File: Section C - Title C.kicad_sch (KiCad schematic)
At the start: 6 parts, among them J11 Conn_01x02_Socket, J2 Conn_01x07_Socket, J6 Conn_01x03_Socket, J7 Conn_01x04_Socket, J8 Conn_01x03_Socket, J9 Conn_01x03_Socket

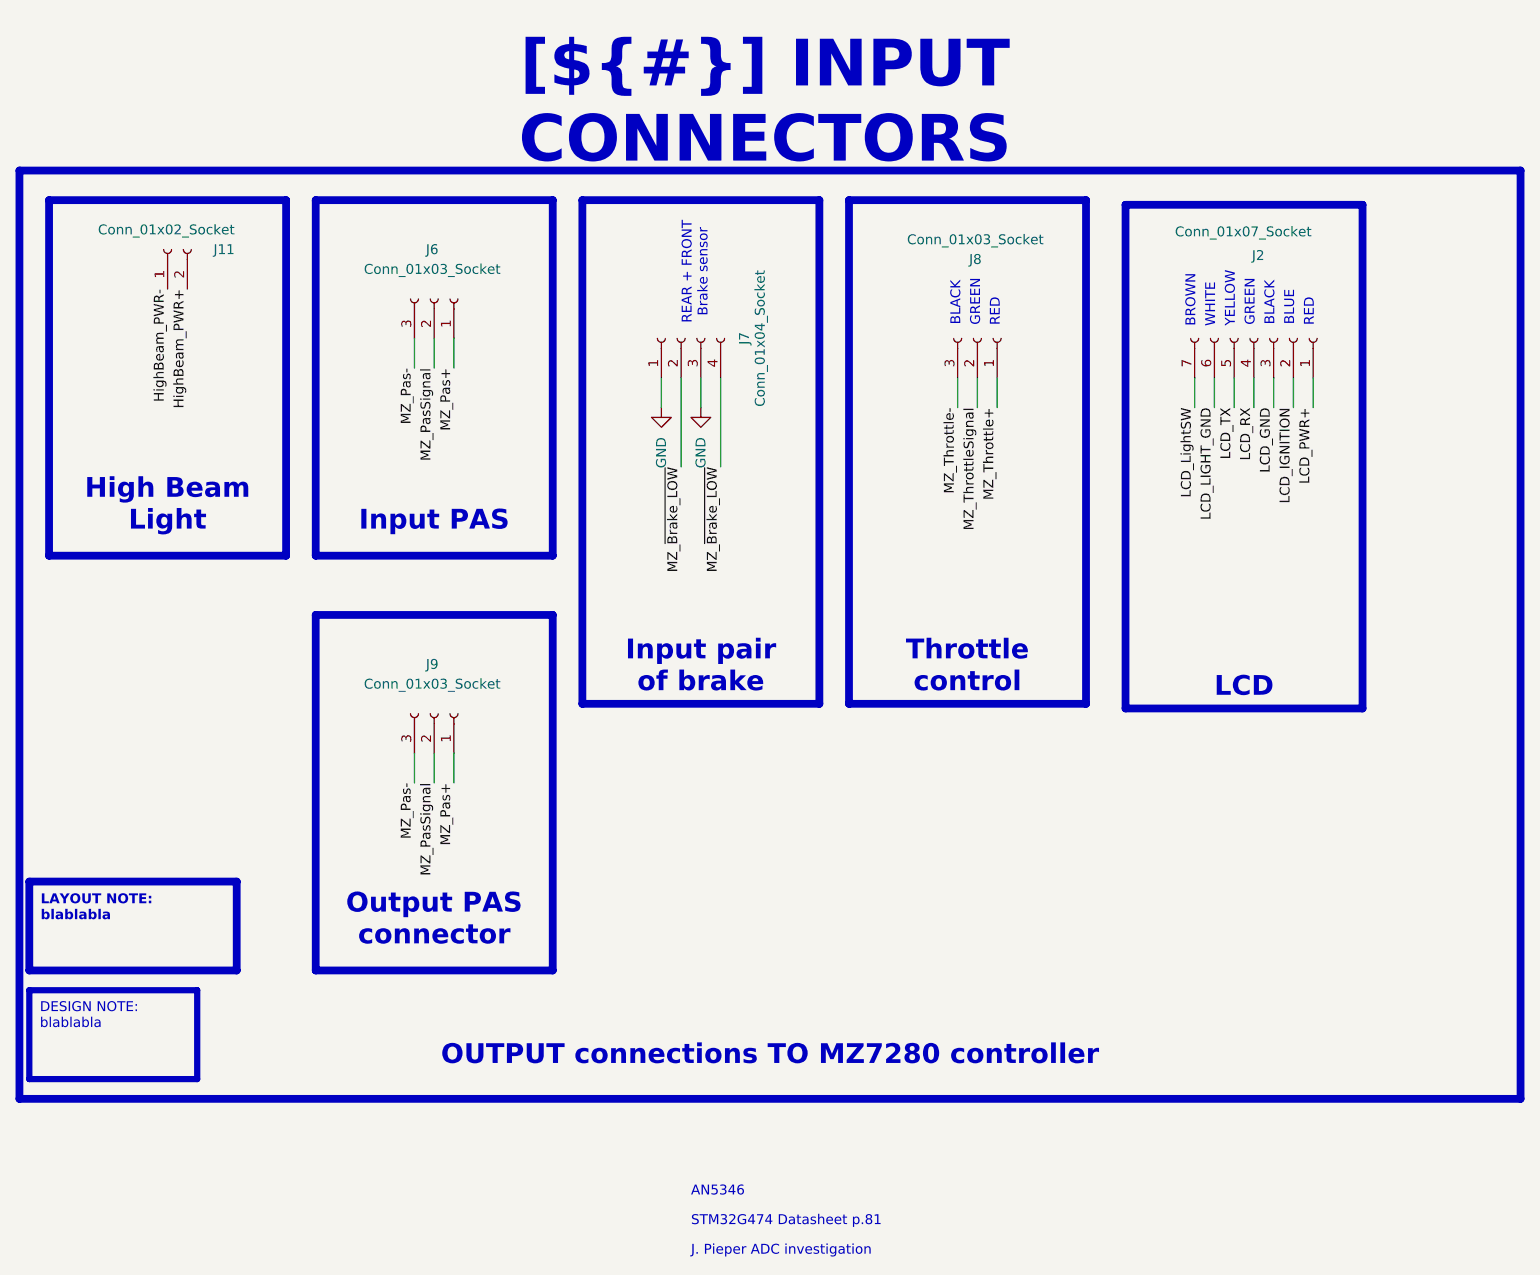
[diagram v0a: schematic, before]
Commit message: [SCHEMATICS] Ajout de convertisseur + autres
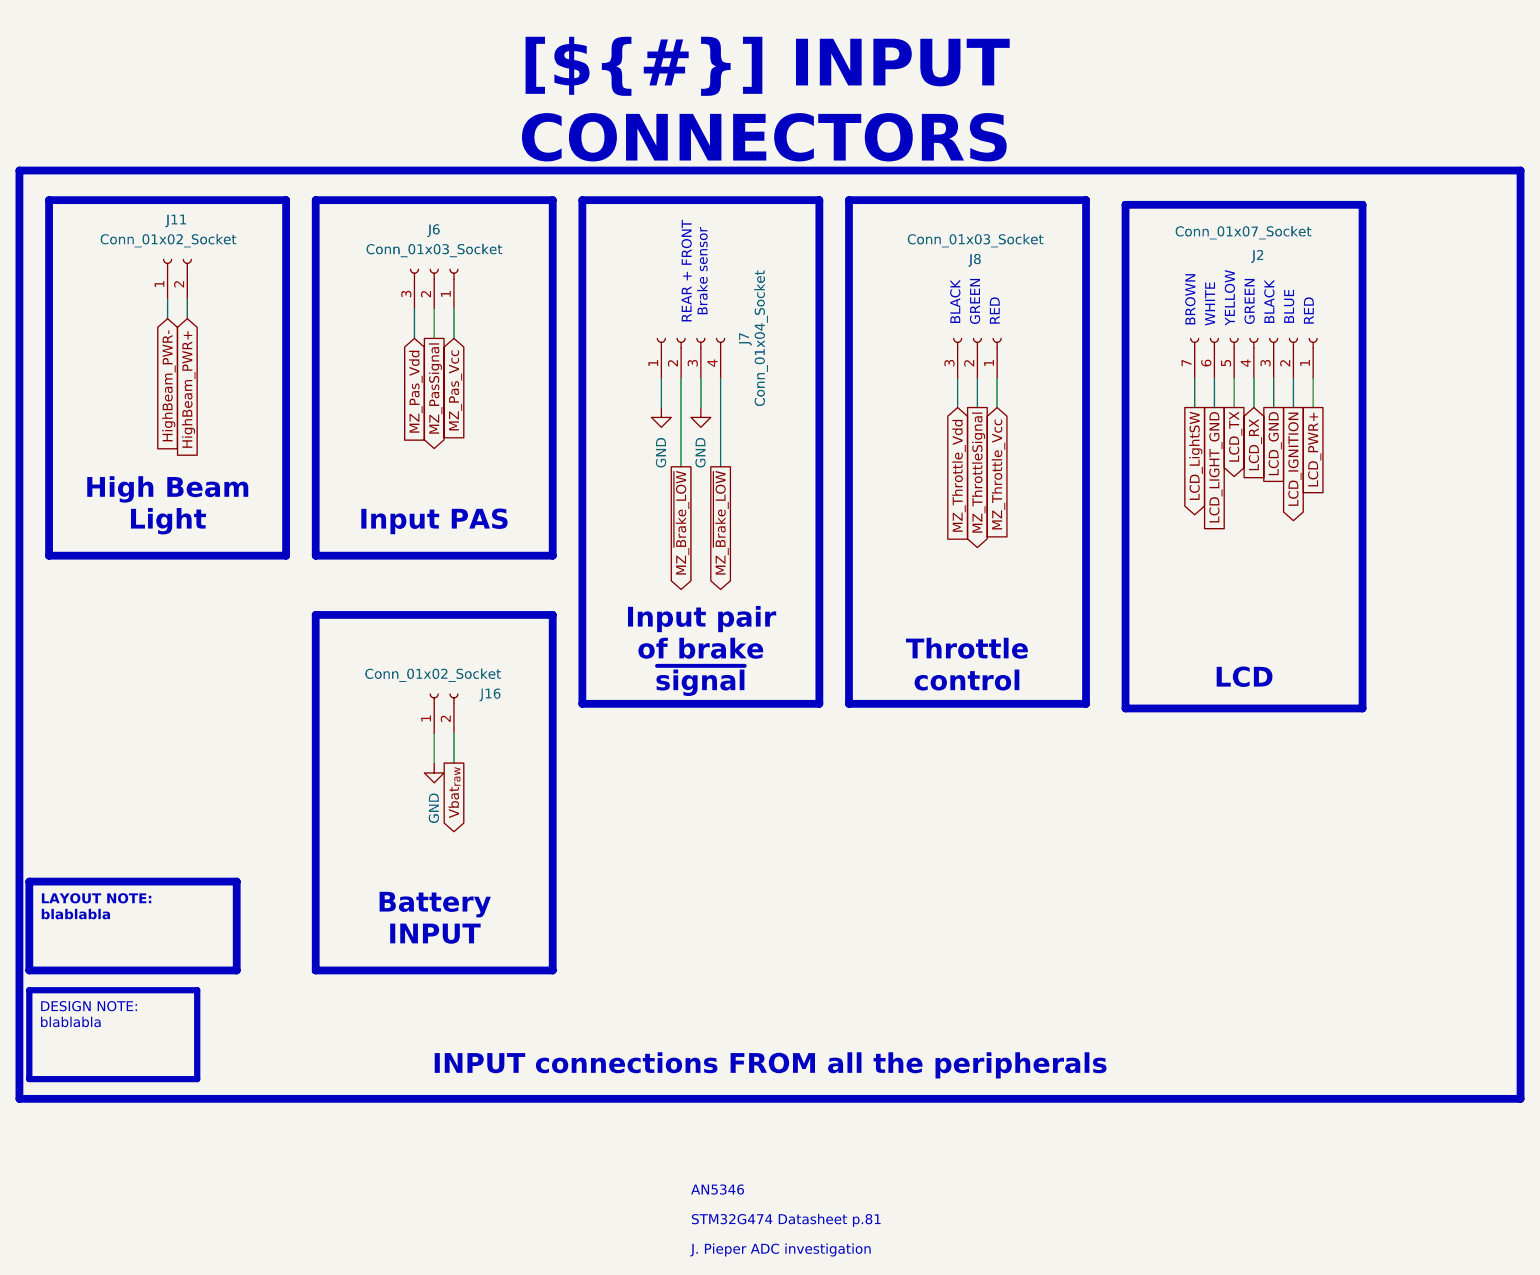
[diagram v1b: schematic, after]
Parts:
- removed J9: Conn_01x03_Socket, symbol Connector:Conn_01x03_Socket
- added J16: Conn_01x02_Socket, symbol Connector:Conn_01x02_Socket
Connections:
- net GND: now also J16.1 (Pin_1)
- net MZ_Pas+ renamed MZ_Pas_Vcc
- net MZ_Pas- renamed MZ_Pas_Vdd
- net MZ_Throttle+ renamed MZ_Throttle_Vcc
- net MZ_Throttle- renamed MZ_Throttle_Vdd
- new net Vbat_{raw}: J16.2 (Pin_2)
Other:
- moved on the sheet: J11, J6
